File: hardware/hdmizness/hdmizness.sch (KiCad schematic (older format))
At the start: 2 parts

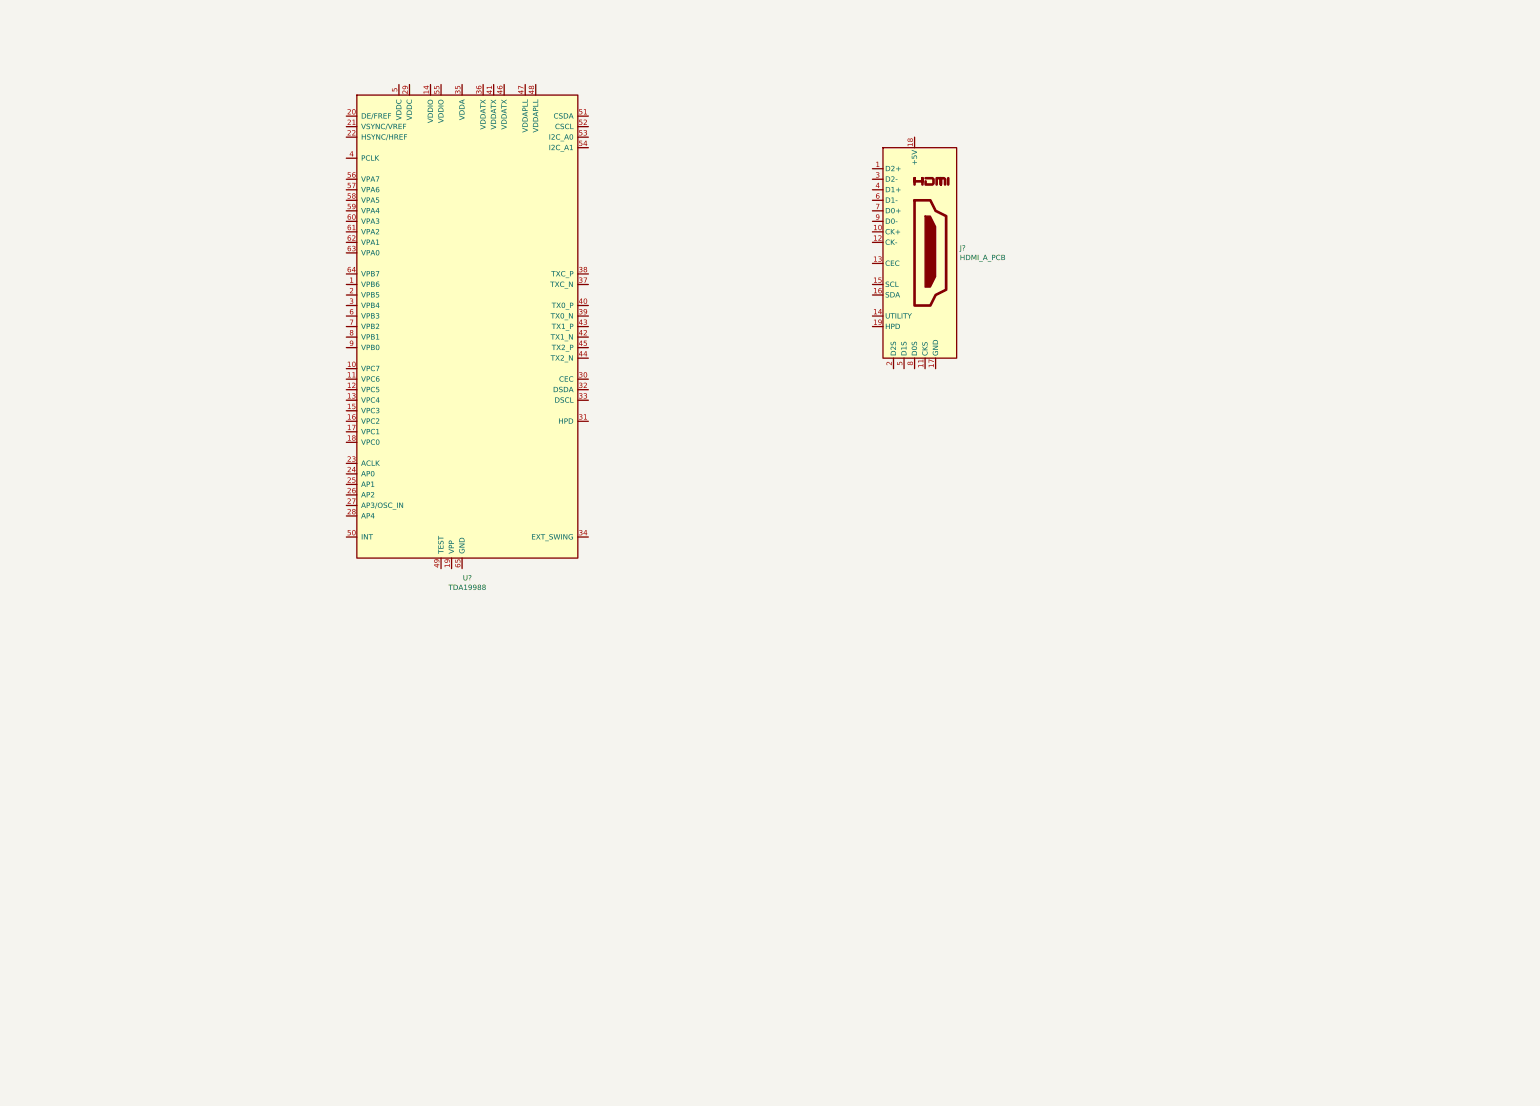
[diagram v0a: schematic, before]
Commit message: hdmizness: Add schematic first draft
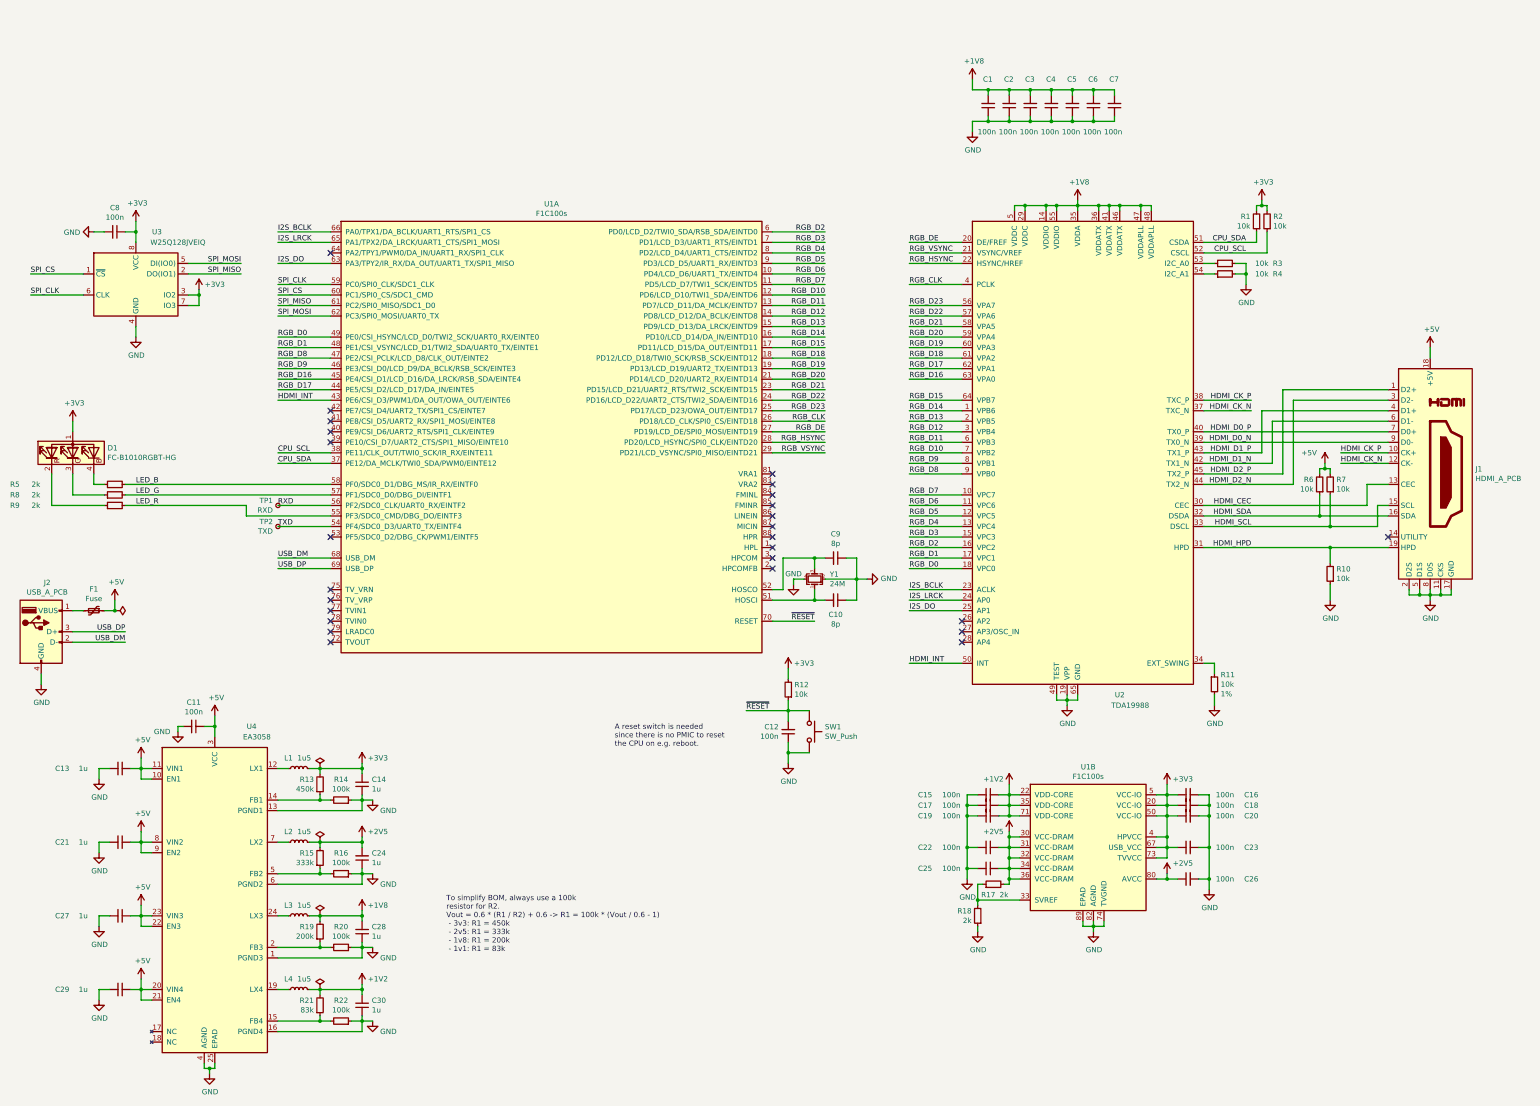
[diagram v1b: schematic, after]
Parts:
- added C1, C11, C12, C15, C16, C17, C18, C19, C2, C20, C22, C23, C25, C26, C3, C4, C5, C6, C7, C8: 100n, Capacitor_SMD:C_0402_1005Metric, symbol Device:C_Small
- added C10, C9: 8p, Capacitor_SMD:C_0402_1005Metric, symbol Device:C_Small
- added C13, C14, C21, C24, C27, C28, C29, C30: 1u, Capacitor_SMD:C_0402_1005Metric, symbol Device:C_Small
- added D1: FC-B1010RGBT-HG, hdmizness:PLCC1010, symbol hdmizness:FC-B1010RGBT-HG
- added F1: Fuse, Fuse:Fuse_0603_1608Metric, symbol Device:Polyfuse_Small
- added J2: USB_A_PCB, hdmizness:USB_A_PCB, symbol hdmizness:USB_A_PCB
- added L1, L2, L3, L4: 1u5, hdmizness:L_Vishay_IHHP-0806, symbol Device:L_Small
- added R1, R10, R11, R12, R2, R3, R4, R6, R7: 10k, Resistor_SMD:R_0402_1005Metric, symbol Device:R_Small
- added R13: 450k, Resistor_SMD:R_0402_1005Metric, symbol Device:R_Small
- added R14, R16, R20, R22: 100k, Resistor_SMD:R_0402_1005Metric, symbol Device:R_Small
- added R15: 333k, Resistor_SMD:R_0402_1005Metric, symbol Device:R_Small
- added R17, R18, R5, R8, R9: 2k, Resistor_SMD:R_0402_1005Metric, symbol Device:R_Small
- added R19: 200k, Resistor_SMD:R_0402_1005Metric, symbol Device:R_Small
- added R21: 83k, Resistor_SMD:R_0402_1005Metric, symbol Device:R_Small
- added SW1: SW_Push, Button_Switch_SMD:SW_SPST_SKQG_WithStem, symbol Switch:SW_Push
- added TP1: RXD, TestPoint:TestPoint_Pad_1.0x1.0mm, symbol Connector:TestPoint_Small
- added TP2: TXD, TestPoint:TestPoint_Pad_1.0x1.0mm, symbol Connector:TestPoint_Small
- added U1: F1C100s, hdmizness:QFN-88_EP_10x10_Pitch0.4mm, symbol hdmizness:F1C100s
- added U3: W25Q128JVEIQ, hdmizness:WSON-8-1EP_8x6mm_P1.27mm_EP3.4x4.3mm, symbol hdmizness:W25Q128JVEIQ
- added U4: EA3058, Package_DFN_QFN:QFN-24-1EP_4x4mm_P0.5mm_EP2.6x2.6mm, symbol hdmizness:EA3058
- added Y1: 24M, Crystal:Crystal_SMD_3225-4Pin_3.2x2.5mm, symbol Device:Crystal_GND24_Small
- gave numbers to parts that had none: 2
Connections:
- net RGB_D14: now reaches U2.1 (VPB6)
- net RGB_D14: now also U1.16 (PD10/LCD_D14/DA_IN/EINTD10)
- net RGB_D7: now reaches U2.10 (VPC7)
- net RGB_D7: now also U1.11 (PD5/LCD_D7/TWI1_SCK/EINTD5)
- net RGB_D6: now reaches U2.11 (VPC6)
- net RGB_D6: now also U1.10 (PD4/LCD_D6/UART1_TX/EINTD4)
- net RGB_D5: now reaches U2.12 (VPC5)
- net RGB_D5: now also U1.9 (PD3/LCD_D5/UART1_RX/EINTD3)
- net RGB_D4: now reaches U2.13 (VPC4)
- net RGB_D4: now also U1.8 (PD2/LCD_D4/UART1_CTS/EINTD2)
- net +1V8: now reaches U2.14 (VDDIO)
- net +1V8: now also U2.29 (VDDC), U2.35 (VDDA), U2.36 (VDDATX), U2.41 (VDDATX), U2.46 (VDDATX), U2.47 (VDDAPLL), U2.48 (VDDAPLL), U2.5 (VDDC), U2.55 (VDDIO), C1.2, C2.2, C28.2, C3.2, C4.2, C5.2, C6.2, C7.2, L3.2, R19.2
- net RGB_D3: now reaches U2.15 (VPC3)
- net RGB_D3: now also U1.7 (PD1/LCD_D3/UART1_RTS/EINTD1)
- net RGB_D2: now reaches U2.16 (VPC2)
- net RGB_D2: now also U1.6 (PD0/LCD_D2/TWI0_SDA/RSB_SDA/EINTD0)
- net RGB_D1: now reaches U2.17 (VPC1)
- net RGB_D1: now also U1.48 (PE1/CSI_VSYNC/LCD_D1/TWI2_SDA/UART0_TX/EINTE1)
- net RGB_D0: now reaches U2.18 (VPC0)
- net RGB_D0: now also U1.49 (PE0/CSI_HSYNC/LCD_D0/TWI2_SCK/UART0_RX/EINTE0)
- net GND: now reaches U2.19 (VPP)
- net GND: now also J1.11 (CKS), J1.17 (GND), J1.2 (D2S), J1.5 (D1S), J1.8 (D0S), U2.49 (TEST), U2.65 (GND), C1.1, C10.1, C11.2, C12.1, C13.2, C14.1, C15.2, C16.2, C17.2, C18.2, C19.2, C2.1, C20.2, C21.2, C22.2, C23.2, C24.1, C25.2, C26.2, C27.2, C28.1, C29.2, C3.1, C30.1, C4.1, C5.1, C6.1, C7.1, C8.2, C9.1, J2.4 (GND), R10.1, R11.2, R14.1, R16.1, R18.1, R20.1, R22.1, R3.2, R4.2, SW1.2, U1.74 (TVGND), U1.82 (AGND), U1.89 (EPAD), U3.4 (GND), U4.1 (PGND3), U4.13 (PGND1), U4.16 (PGND4), U4.25 (EPAD), U4.4 (AGND), U4.6 (PGND2), Y1.2, Y1.4
- net RGB_D13: now reaches U2.2 (VPB5)
- net RGB_D13: now also U1.15 (PD9/LCD_D13/DA_LRCK/EINTD9)
- net RGB_DE: now reaches U2.20 (DE/FREF)
- net RGB_DE: now also U1.27 (PD19/LCD_DE/SPI0_MOSI/EINTD19)
- net RGB_VSYNC: now reaches U2.21 (VSYNC/VREF)
- net RGB_VSYNC: now also U1.29 (PD21/LCD_VSYNC/SPI0_MISO/EINTD21)
- net RGB_HSYNC: now reaches U2.22 (HSYNC/HREF)
- net RGB_HSYNC: now also U1.28 (PD20/LCD_HSYNC/SPI0_CLK/EINTD20)
- net I2S_BCLK: now reaches U2.23 (ACLK)
- net I2S_BCLK: now also U1.66 (PA0/TPX1/DA_BCLK/UART1_RTS/SPI1_CS)
- net I2S_LRCK: now reaches U2.24 (AP0)
- net I2S_LRCK: now also U1.65 (PA1/TPX2/DA_LRCK/UART1_CTS/SPI1_MOSI)
- net I2S_DO: now reaches U2.25 (AP1)
- net I2S_DO: now also U1.63 (PA3/TPY2/IR_RX/DA_OUT/UART1_TX/SPI1_MISO)
- net RGB_D12: now reaches U2.3 (VPB4)
- net RGB_D12: now also U1.14 (PD8/LCD_D12/DA_BCLK/EINTD8)
- net HDMI_CEC: now reaches U2.30 (CEC)
- net HDMI_CEC: now also J1.13 (CEC)
- net HDMI_HPD: now reaches U2.31 (HPD)
- net HDMI_HPD: now also J1.19 (HPD), R10.2
- net HDMI_SDA: now reaches U2.32 (DSDA)
- net HDMI_SDA: now also J1.16 (SDA), R6.1
- net HDMI_SCL: now reaches U2.33 (DSCL)
- net HDMI_SCL: now also J1.15 (SCL), R7.1
- net at U2.34 (EXT_SWING): now also R11.1
- net HDMI_CK_N: now reaches U2.37 (TXC_N)
- net HDMI_CK_N: now also J1.12 (CK-)
- net HDMI_CK_P: now reaches U2.38 (TXC_P)
- net HDMI_CK_P: now also J1.10 (CK+)
- net HDMI_D0_N: now reaches U2.39 (TX0_N)
- net HDMI_D0_N: now also J1.9 (D0-)
- net RGB_CLK: now reaches U2.4 (PCLK)
- net RGB_CLK: now also U1.26 (PD18/LCD_CLK/SPI0_CS/EINTD18)
- net HDMI_D0_P: now reaches U2.40 (TX0_P)
- net HDMI_D0_P: now also J1.7 (D0+)
- net HDMI_D1_N: now reaches U2.42 (TX1_N)
- net HDMI_D1_N: now also J1.6 (D1-)
- net HDMI_D1_P: now reaches U2.43 (TX1_P)
- net HDMI_D1_P: now also J1.4 (D1+)
- net HDMI_D2_N: now reaches U2.44 (TX2_N)
- net HDMI_D2_N: now also J1.3 (D2-)
- net HDMI_D2_P: now reaches U2.45 (TX2_P)
- net HDMI_D2_P: now also J1.1 (D2+)
- net HDMI_INT: now reaches U2.50 (INT)
- net HDMI_INT: now also U1.43 (PE6/CSI_D3/PWM1/DA_OUT/OWA_OUT/EINTE6)
- net CPU_SDA: now reaches U2.51 (CSDA)
- net CPU_SDA: now also R1.1, U1.37 (PE12/DA_MCLK/TWI0_SDA/PWM0/EINTE12)
- net CPU_SCL: now reaches U2.52 (CSCL)
- net CPU_SCL: now also R2.1, U1.38 (PE11/CLK_OUT/TWI0_SCK/IR_RX/EINTE11)
- net at U2.53 (I2C_A0): now also R3.1
- net at U2.54 (I2C_A1): now also R4.1
- net RGB_D23: now reaches U2.56 (VPA7)
- net RGB_D23: now also U1.25 (PD17/LCD_D23/OWA_OUT/EINTD17)
- net RGB_D22: now reaches U2.57 (VPA6)
- net RGB_D22: now also U1.24 (PD16/LCD_D22/UART2_CTS/TWI2_SDA/EINTD16)
- net RGB_D21: now reaches U2.58 (VPA5)
- net RGB_D21: now also U1.23 (PD15/LCD_D21/UART2_RTS/TWI2_SCK/EINTD15)
- net RGB_D20: now reaches U2.59 (VPA4)
- net RGB_D20: now also U1.21 (PD14/LCD_D20/UART2_RX/EINTD14)
- net RGB_D11: now reaches U2.6 (VPB3)
- net RGB_D11: now also U1.13 (PD7/LCD_D11/DA_MCLK/EINTD7)
- net RGB_D19: now reaches U2.60 (VPA3)
- net RGB_D19: now also U1.19 (PD13/LCD_D19/UART2_TX/EINTD13)
- net RGB_D18: now reaches U2.61 (VPA2)
- net RGB_D18: now also U1.18 (PD12/LCD_D18/TWI0_SCK/RSB_SCK/EINTD12)
- net RGB_D17: now reaches U2.62 (VPA1)
- net RGB_D17: now also U1.44 (PE5/CSI_D2/LCD_D17/DA_IN/EINTE5)
- net RGB_D16: now reaches U2.63 (VPA0)
- net RGB_D16: now also U1.45 (PE4/CSI_D1/LCD_D16/DA_LRCK/RSB_SDA/EINTE4)
- net RGB_D15: now reaches U2.64 (VPB7)
- net RGB_D15: now also U1.17 (PD11/LCD_D15/DA_OUT/EINTD11)
- net RGB_D10: now reaches U2.7 (VPB2)
- net RGB_D10: now also U1.12 (PD6/LCD_D10/TWI1_SDA/EINTD6)
- net RGB_D9: now reaches U2.8 (VPB1)
- net RGB_D9: now also U1.46 (PE3/CSI_D0/LCD_D9/DA_BCLK/RSB_SCK/EINTE3)
- net RGB_D8: now reaches U2.9 (VPB0)
- net RGB_D8: now also U1.47 (PE2/CSI_PCLK/LCD_D8/CLK_OUT/EINTE2)
- net +5V: now reaches J1.18 (+5V)
- net +5V: now also C11.1, C13.1, C21.1, C27.1, C29.1, F1.1, R6.2, R7.2, U4.10 (EN1), U4.11 (VIN1), U4.20 (VIN4), U4.21 (EN4), U4.22 (EN3), U4.23 (VIN3), U4.3 (VCC), U4.8 (VIN2), U4.9 (EN2)
- new net: C10.2, U1.51 (HOSCI), Y1.1
- new net: C9.2, U1.52 (HOSCO), Y1.3
- new net: R17.1, R18.2, U1.33 (SVREF)
- new net: L1.1, U4.12 (LX1)
- new net: R13.1, R14.2, U4.14 (FB1)
- new net: R21.1, R22.2, U4.15 (FB4)
- new net: L4.1, U4.19 (LX4)
- new net: R19.1, R20.2, U4.2 (FB3)
- new net: L3.1, U4.24 (LX3)
- new net: R15.1, R16.2, U4.5 (FB2)
- new net: L2.1, U4.7 (LX2)
- new net: D1.2 (RK), R9.1
- new net: D1.3 (GK), R8.1
- new net: D1.4 (BK), R5.1
- new net: F1.2, J2.1 (VBUS)
- new net +1V2: C15.1, C17.1, C19.1, C30.2, L4.2, R21.2, U1.22 (VDD-CORE), U1.35 (VDD-CORE), U1.71 (VDD-CORE)
- new net +2V5: C22.1, C24.2, C25.1, C26.1, L2.2, R15.2, R17.2, U1.30 (VCC-DRAM), U1.31 (VCC-DRAM), U1.32 (VCC-DRAM), U1.34 (VCC-DRAM), U1.36 (VCC-DRAM), U1.80 (AVCC)
- new net +3V3: C14.2, C16.1, C18.1, C20.1, C23.1, C8.1, D1.1 (A), L1.2, R1.2, R12.2, R13.2, R2.2, U1.20 (VCC-IO), U1.4 (HPVCC), U1.5 (VCC-IO), U1.50 (VCC-IO), U1.67 (USB_VCC), U1.73 (TVVCC), U3.3 (IO2), U3.7 (IO3), U3.8 (VCC)
- new net LED_B: R5.2, U1.58 (PF0/SDC0_D1/DBG_MS/IR_RX/EINTF0)
- new net LED_G: R8.2, U1.57 (PF1/SDC0_D0/DBG_DI/EINTF1)
- new net LED_R: R9.2, U1.55 (PF3/SDC0_CMD/DBG_DO/EINTF3)
- new net RXD: TP1.1, U1.56 (PF2/SDC0_CLK/UART0_RX/EINTF2)
- new net SPI_CLK: U1.59 (PC0/SPI0_CLK/SDC1_CLK), U3.6 (CLK)
- new net SPI_CS: U1.60 (PC1/SPI0_CS/SDC1_CMD), U3.1 (~CS)
- new net SPI_MISO: U1.61 (PC2/SPI0_MISO/SDC1_D0), U3.2 (DO(IO1))
- new net SPI_MOSI: U1.62 (PC3/SPI0_MOSI/UART0_TX), U3.5 (DI(IO0))
- new net TXD: TP2.1, U1.54 (PF4/SDC0_D3/UART0_TX/EINTF4)
- new net USB_DM: J2.2 (D-), U1.68 (USB_DM)
- new net USB_DP: J2.3 (D+), U1.69 (USB_DP)
- new net ~RESET: C12.2, R12.1, SW1.1, U1.70 (RESET)
- no-connect marks 0 -> 26
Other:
- note added: "A reset switch is needed\nsince there is no PMIC to reset\nthe CPU on e.g. reboot."
- note added: "To simplify BOM, always use a 100k\nresistor for R2.\nVout = 0.6 * (R1 / R2) + 0.6 -> R1 = 100k * (Vout / 0.6 - 1)\n - 3v3: R1 = 450k\n - 2v5: R1 = 333k\n - 1v8: R1 = 200k\n - 1v1: R1 = 83k"
- moved on the sheet: J1, U2

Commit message: hdmizness: Use smaller components
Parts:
- SW1: footprint Button_Switch_SMD:SW_SPST_SKQG_WithStem -> hdmizness:1TS028A-2400-0603-CT; LCSC P/N (none) -> C481994; MFR P/N (none) -> 1TS028A-2400-0603-CT
- U4: LCSC P/N (none) -> C575412; MFR P/N (none) -> EA3058QDR
- Y1: footprint Crystal:Crystal_SMD_3225-4Pin_3.2x2.5mm -> Crystal:Crystal_SMD_2016-4Pin_2.0x1.6mm; LCSC P/N C709181 -> C708986; MFR P/N JF4024M00009T8188070 -> CN4024M00009T8188011
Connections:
- net USB_DM renamed USB_DN
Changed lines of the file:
@@
 USB_DP
 Text Label 3550 5850 0    50   ~ 0
-USB_DM
+USB_DN
 Wire Wire Line
 	4050 4350 3550 4350
@@
 F 0 "Y1" V 8696 5906 50  0000 R CNN
 F 1 "24M" V 8605 5906 50  0000 R CNN
-F 2 "Crystal:Crystal_SMD_3225-4Pin_3.2x2.5mm" V 8559 5906 50  0001 R CNN
+F 2 "Crystal:Crystal_SMD_2016-4Pin_2.0x1.6mm" V 8559 5906 50  0001 R CNN
 F 3 "~" H 8650 6050 50  0001 C CNN
-F 4 "C709181" H 8650 6050 50  0001 C CNN "LCSC P/N"
-F 5 "JF4024M00009T8188070" H 8650 6050 50  0001 C CNN "MFR P/N"
+F 4 "C708986" H 8650 6050 50  0001 C CNN "LCSC P/N"
+F 5 "CN4024M00009T8188011" H 8650 6050 50  0001 C CNN "MFR P/N"
 	1    8650 6050
 	0    -1   -1   0
@@
 F 0 "SW1" V 8554 7648 50  0000 L CNN
 F 1 "SW_Push" V 8645 7648 50  0000 L CNN
-F 2 "Button_Switch_SMD:SW_SPST_SKQG_WithStem" H 8600 7700 50  0001 C CNN
+F 2 "hdmizness:1TS028A-2400-0603-CT" H 8600 7700 50  0001 C CNN
 F 3 "~" H 8600 7700 50  0001 C CNN
+F 4 "C481994" H 8600 7500 50  0001 C CNN "LCSC P/N"
+F 5 "1TS028A-2400-0603-CT" H 8600 7500 50  0001 C CNN "MFR P/N"
 	1    8600 7500
 	0    1    1    0
@@
 Wire Wire Line
 	8400 7700 8400 7800
-Text Notes 6750 7650 0    50   ~ 0
-A reset switch is needed\nsince there is no PMIC to reset\nthe CPU on e.g. reboot.
 $Comp
 L power:+3V3 #PWR08
@@
 F 2 "Package_DFN_QFN:QFN-24-1EP_4x4mm_P0.5mm_EP2.6x2.6mm" H 2450 7650 50  0001 C CNN
 F 3 "https://datasheet.lcsc.com/szlcsc/2006041834_Everanalog-IC-design-EA3058QDR_C575412.pdf" H 2450 7650 50  0001 C CNN
+F 4 "C575412" H 2450 7650 50  0001 C CNN "LCSC P/N"
+F 5 "EA3058QDR" H 2450 7650 50  0001 C CNN "MFR P/N"
 	1    2450 7650
 	1    0    0    -1
@@
 USB_DP
 Text Label 2100 6650 2    50   ~ 0
-USB_DM
+USB_DN
 $Comp
 L Device:Polyfuse_Small F1
@@
 	1    0    0    1
 $EndComp
+Text Notes 6750 7650 0    50   ~ 0
+A reset switch is needed\nsince there is no PMIC to reset\nthe CPU on e.g. reboot.
 $EndSCHEMATC

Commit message: hdmizness: Routing done
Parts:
- removed C1: 100n, Capacitor_SMD:C_0402_1005Metric, symbol Device:C_Small
- removed R3, R4: 10k, Resistor_SMD:R_0402_1005Metric, symbol Device:R_Small
- removed U3: W25Q128JVEIQ, hdmizness:WSON-8-1EP_8x6mm_P1.27mm_EP3.4x4.3mm, symbol hdmizness:W25Q128JVEIQ
- added U3: W25Q128JVPIQ, Package_SON:WSON-8-1EP_6x5mm_P1.27mm_EP3.4x4.3mm, symbol hdmizness:W25Q128JVPIQ
- R15: value 333k -> 200k
- R19: value 200k -> 333k
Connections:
- net +1V8: now also C24.2, L2.2, R15.2; no longer C28.2, L3.2, R19.2
- net +2V5: now also C28.2, L3.2, R19.2; no longer C24.2, L2.2, R15.2
- net +3V3: now also U3.3 (IO2), U3.7 (IO3), U3.8 (VCC)
- net GND: now also U2.17 (VPC1), U2.18 (VPC0), U2.53 (I2C_A0), U2.54 (I2C_A1), U2.62 (VPA1), U2.63 (VPA0), U2.8 (VPB1), U2.9 (VPB0), U3.4 (GND)
- net SPI_CLK: now also U3.6 (CLK)
- net SPI_CS: now also U3.1 (~CS)
- net SPI_MISO: now also U3.2 (DO(IO1))
- net SPI_MOSI: now also U3.5 (DI(IO0))
- net RGB_D0: no longer names the net of U1.49 (PE0/CSI_HSYNC/LCD_D0/TWI2_SCK/UART0_RX/EINTE0)
- net RGB_D0: no longer U2.18 (VPC0)
- net RGB_D1: no longer names the net of U1.48 (PE1/CSI_VSYNC/LCD_D1/TWI2_SDA/UART0_TX/EINTE1)
- net RGB_D1: no longer U2.17 (VPC1)
- net RGB_D16: no longer names the net of U1.45 (PE4/CSI_D1/LCD_D16/DA_LRCK/RSB_SDA/EINTE4)
- net RGB_D16: no longer U2.63 (VPA0)
- net RGB_D17: no longer names the net of U1.44 (PE5/CSI_D2/LCD_D17/DA_IN/EINTE5)
- net RGB_D17: no longer U2.62 (VPA1)
- net RGB_D8: no longer names the net of U1.47 (PE2/CSI_PCLK/LCD_D8/CLK_OUT/EINTE2)
- net RGB_D8: no longer U2.9 (VPB0)
- net RGB_D9: no longer names the net of U1.46 (PE3/CSI_D0/LCD_D9/DA_BCLK/RSB_SCK/EINTE3)
- net RGB_D9: no longer U2.8 (VPB1)
- no-connect marks 26 -> 32

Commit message: hdmizness: Add board revision hard straps
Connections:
- net +3V3: now also U1.49 (PE0/CSI_HSYNC/LCD_D0/TWI2_SCK/UART0_RX/EINTE0)
- net GND: now also U1.44 (PE5/CSI_D2/LCD_D17/DA_IN/EINTE5), U1.45 (PE4/CSI_D1/LCD_D16/DA_LRCK/RSB_SDA/EINTE4), U1.46 (PE3/CSI_D0/LCD_D9/DA_BCLK/RSB_SCK/EINTE3), U1.47 (PE2/CSI_PCLK/LCD_D8/CLK_OUT/EINTE2), U1.48 (PE1/CSI_VSYNC/LCD_D1/TWI2_SDA/UART0_TX/EINTE1)
- net HDMI_INT: now also U1.39 (PE10/CSI_D7/UART2_CTS/SPI1_MISO/EINTE10); no longer U1.43 (PE6/CSI_D3/PWM1/DA_OUT/OWA_OUT/EINTE6)
- no-connect marks 32 -> 26
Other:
- note added: "0"
- note added: "1"
- note added: "2"
- note added: "Board revision\nhard straps"
- note added: "Major"
- note added: "Minor"
- note added: "v1.0"
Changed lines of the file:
@@
-$Comp
-L hdmizness:F1C100s U1
-U 1 1 5FA908A0
-P 4150 2650
-F 0 "U1" H 6150 2815 50  0000 C CNN
-F 1 "F1C100s" H 6150 2724 50  0000 C CNN
-F 2 "hdmizness:QFN-88_EP_10x10_Pitch0.4mm" H 4150 2650 50  0001 C CNN
-F 3 "https://linux-sunxi.org/images/b/ba/F1C100s_Datasheet_V1.0.pdf" H 4150 2650 50  0001 C CNN
-	1    4150 2650
-	1    0    0    -1
-$EndComp
 $Comp
 L hdmizness:F1C100s U1
@@
 Text Label 3550 5850 0    50   ~ 0
 USB_DN
-Wire Wire Line
-	4050 4350 3550 4350
-Text Label 3550 4350 0    50   ~ 0
-HDMI_INT
 NoConn ~ 4050 6150
 NoConn ~ 4050 6250
@@
 NoConn ~ 4050 4550
 NoConn ~ 4050 4650
-NoConn ~ 4050 4750
 NoConn ~ 4050 2950
 $Comp
@@
 	8250 2150 8250 2250
 $Comp
-L power:GND #PWR?
+L power:GND #PWR0101
 U 1 1 61F1EB39
 P 8250 2250
-F 0 "#PWR?" H 8250 2000 50  0001 C CNN
+F 0 "#PWR0101" H 8250 2000 50  0001 C CNN
 F 1 "GND" H 8255 2077 50  0000 C CNN
 F 2 "" H 8250 2250 50  0001 C CNN
@@
 	-1   0    0    -1
 $EndComp
-NoConn ~ 4050 3750
-NoConn ~ 4050 3850
-NoConn ~ 4050 3950
-NoConn ~ 4050 4050
-NoConn ~ 4050 4150
-NoConn ~ 4050 4250
 Entry Wire Line
 	8750 4850 8850 4750
@@
 Wire Bus Line
 	8850 1750 9450 1750
+Text Label 3550 4750 0    50   ~ 0
+HDMI_INT
+Wire Wire Line
+	4050 4750 3550 4750
+$Comp
+L hdmizness:F1C100s U1
+U 1 1 5FA908A0
+P 4150 2650
+F 0 "U1" H 6150 2815 50  0000 C CNN
+F 1 "F1C100s" H 6150 2724 50  0000 C CNN
+F 2 "hdmizness:QFN-88_EP_10x10_Pitch0.4mm" H 4150 2650 50  0001 C CNN
+F 3 "https://linux-sunxi.org/images/b/ba/F1C100s_Datasheet_V1.0.pdf" H 4150 2650 50  0001 C CNN
+	1    4150 2650
+	1    0    0    -1
+$EndComp
+$Comp
+L power:+3V3 #PWR?
+U 1 1 627DC501
+P 3950 3700
+F 0 "#PWR?" H 3950 3550 50  0001 C CNN
+F 1 "+3V3" H 4100 3750 50  0000 C CNN
+F 2 "" H 3950 3700 50  0001 C CNN
+F 3 "" H 3950 3700 50  0001 C CNN
+	1    3950 3700
+	-1   0    0    -1
+$EndComp
+Wire Wire Line
+	3950 3700 3950 3750
+Wire Wire Line
+	3950 3750 4050 3750
+$Comp
+L power:GND #PWR?
+U 1 1 6281590E
+P 3850 4400
+F 0 "#PWR?" H 3850 4150 50  0001 C CNN
+F 1 "GND" H 3700 4350 50  0000 C CNN
+F 2 "" H 3850 4400 50  0001 C CNN
+F 3 "" H 3850 4400 50  0001 C CNN
+	1    3850 4400
+	1    0    0    -1
+$EndComp
+Wire Wire Line
+	3850 3850 4050 3850
+Wire Wire Line
+	3850 4400 3850 4250
+NoConn ~ 4050 4350
+Wire Wire Line
+	4050 3950 3850 3950
+Connection ~ 3850 3950
+Wire Wire Line
+	3850 3950 3850 3850
+Wire Wire Line
+	4050 4050 3850 4050
+Connection ~ 3850 4050
+Wire Wire Line
+	3850 4050 3850 3950
+Connection ~ 3850 4150
+Wire Wire Line
+	3850 4150 3850 4050
+Wire Wire Line
+	3850 4150 4050 4150
+Wire Wire Line
+	4050 4250 3850 4250
+Connection ~ 3850 4250
+Wire Wire Line
+	3850 4250 3850 4150
+Text Notes 3650 3750 2    50   ~ 0
+0
+Text Notes 3650 3850 2    50   ~ 0
+1
+Text Notes 3650 3950 2    50   ~ 0
+2
+Text Notes 3650 4050 2    50   ~ 0
+0
+Text Notes 3650 4150 2    50   ~ 0
+1
+Text Notes 3650 4250 2    50   ~ 0
+2
+Wire Notes Line
+	3550 3700 3500 3750
+Wire Notes Line
+	3550 3950 3500 3900
+Wire Notes Line
+	3500 3750 3500 3900
+Wire Notes Line
+	3550 4250 3500 4200
+Text Notes 3250 3850 0    50   ~ 0
+Major
+Text Notes 3250 4150 0    50   ~ 0
+Minor
+Text Notes 3000 4500 0    50   ~ 0
+Board revision\nhard straps
+Wire Notes Line
+	3500 4050 3500 4200
+Wire Notes Line
+	3550 4000 3500 4050
 Wire Bus Line
 	8850 1750 8850 4750
 Wire Bus Line
 	9450 1750 9450 5850
+Text Notes 3050 4000 0    50   ~ 0
+v1.0
 $EndSCHEMATC

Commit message: hdmizness/sch: Add component MFR P/N and LCSC P/N
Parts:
- C10, C9: LCSC P/N (none) -> C318586; MFR P/N (none) -> CL05C080CB5NNNC
- C11, C12, C15, C16, C17, C18, C19, C2, C20, C22, C23, C25, C26, C3, C4, C5, C6, C7, C8: LCSC P/N (none) -> C1525; MFR P/N (none) -> CL05B104KO5NNNC
- C13, C14, C21, C24, C27, C28, C29, C30: LCSC P/N (none) -> C107372; MFR P/N (none) -> CL05A105KQ5NNNC
- F1: LCSC P/N (none) -> C182303; MFR P/N (none) -> 06H1100D
- L1, L2, L3, L4: LCSC P/N (none) -> C307630; MFR P/N (none) -> CIGT201610UM1R5MNE
- R1, R10, R11, R12, R2, R6, R7: LCSC P/N (none) -> C406733; MFR P/N (none) -> CR-02FL6---10K
- R13: LCSC P/N (none) -> C407681; MFR P/N (none) -> 0402WGF4503TCE
- R14, R16, R20, R22: LCSC P/N (none) -> C258090; MFR P/N (none) -> RC-02W1003FT
- R15: LCSC P/N (none) -> C305297; MFR P/N (none) -> WR04X2003FTL
- R17, R18, R5, R8, R9: LCSC P/N (none) -> C304583; MFR P/N (none) -> RC-02W2001FT
- R19: LCSC P/N (none) -> C172051; MFR P/N (none) -> WR04X3323FTL
- R21: LCSC P/N (none) -> C304638; MFR P/N (none) -> RC-02W8202FT
